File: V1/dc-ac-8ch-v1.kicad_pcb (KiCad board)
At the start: 2 copper layers, 98 x 67.8 mm, 103 parts, among them J1 DB142V-5.08-4P, J2 DB142V-5.08-4P, J3 DB142V-5.08-2P, J4 DB142V-5.08-4P, J5 DB142V-5.08-4P, J6 DB142V-5.08-2P, U1 MOC3063S, U2 MOC3063S, U3 MOC3063S, U4 MOC3063S, U5 MOC3063S, U6 MOC3063S, U7 MOC3063S, U8 MOC3063S

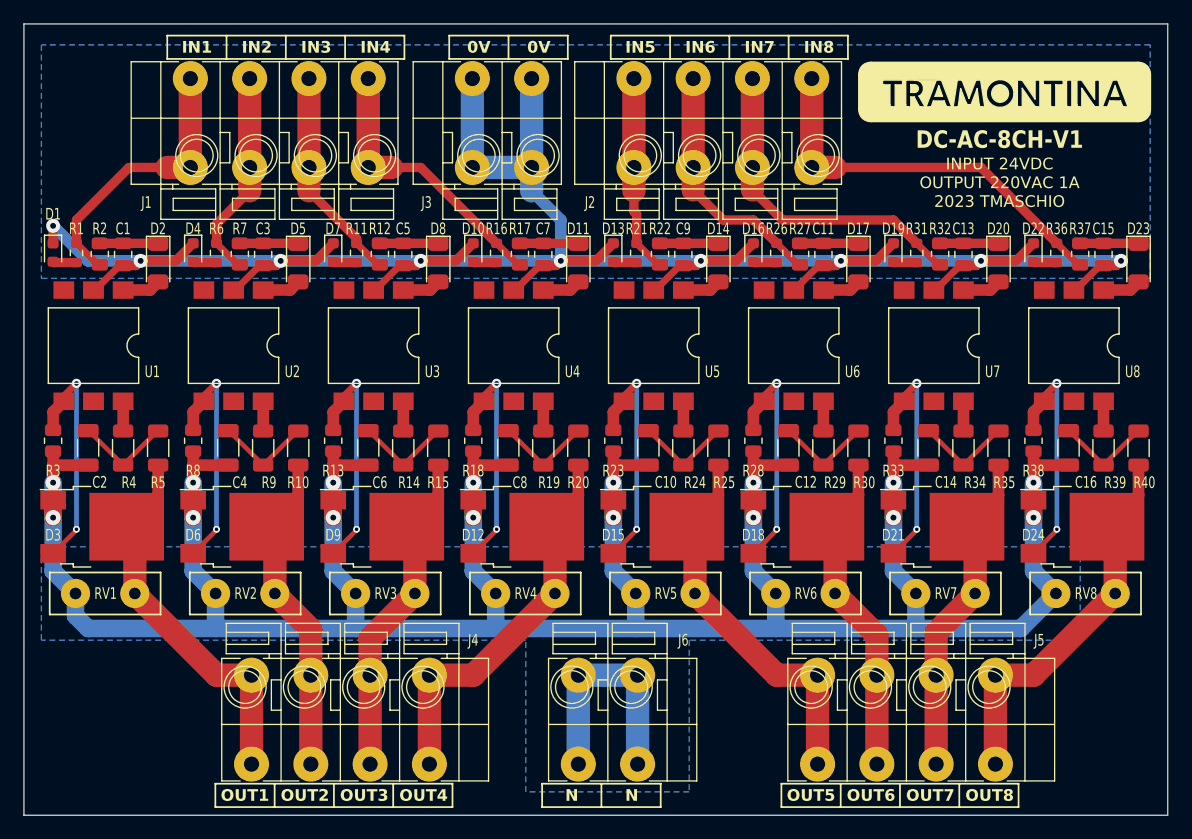
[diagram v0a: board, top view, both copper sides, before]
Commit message: Place missing track under zone
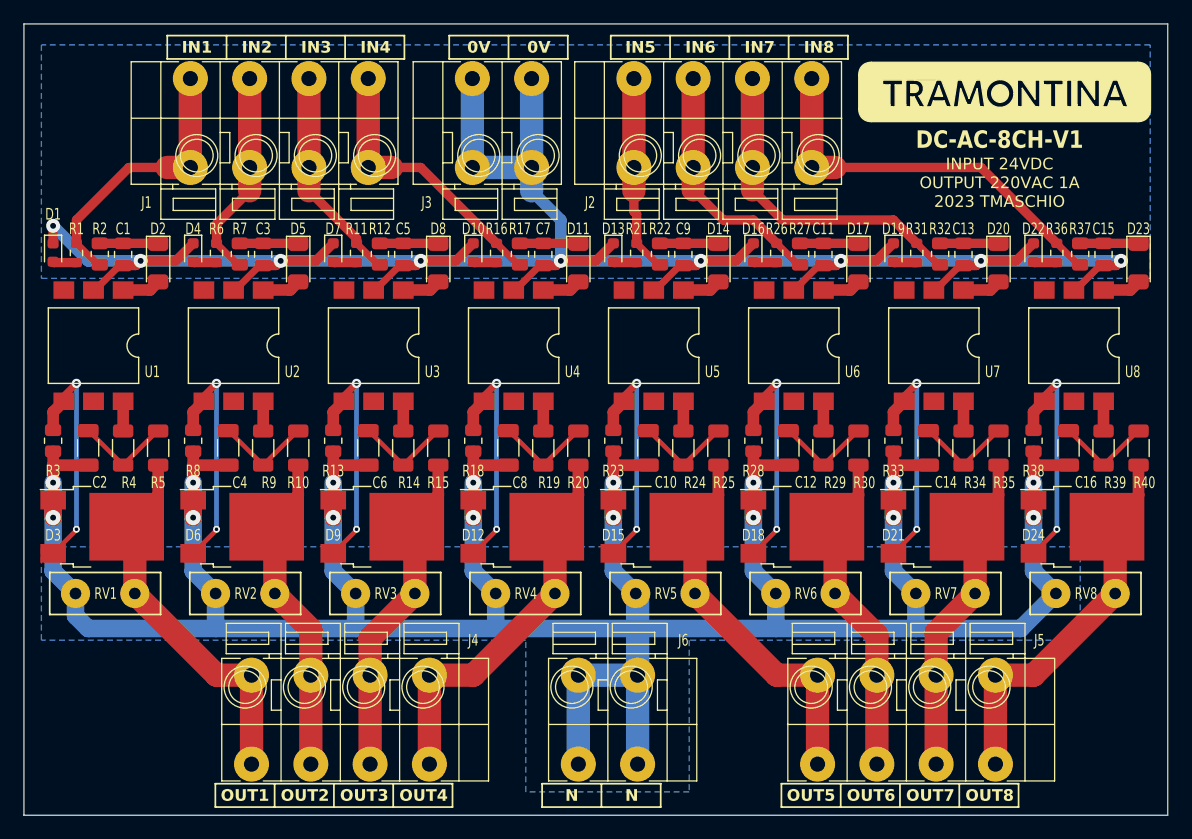
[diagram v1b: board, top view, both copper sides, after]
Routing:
- net NEUTRAL: track 277.7 -> 281.8 mm

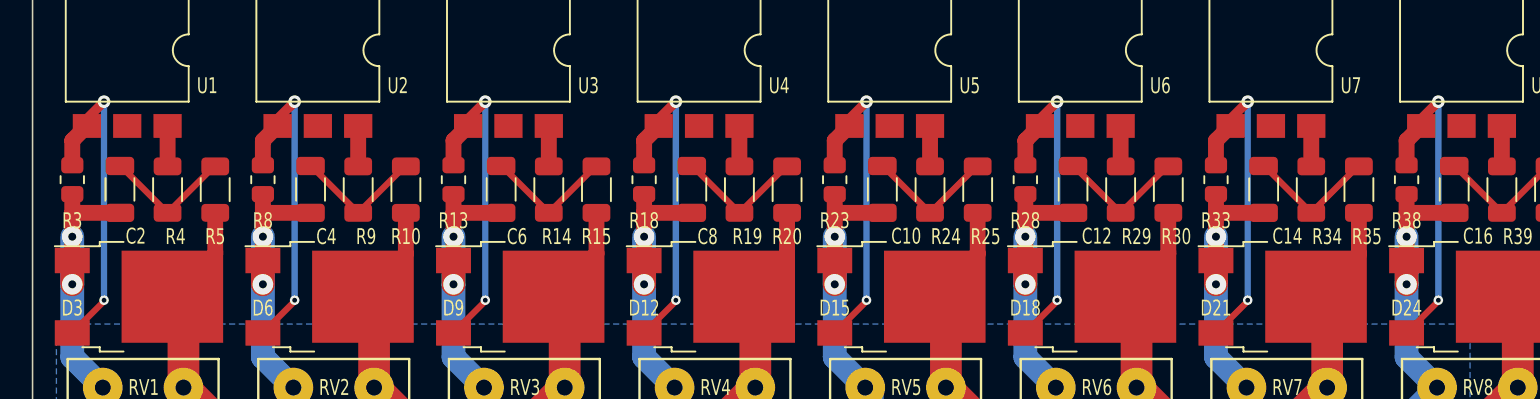
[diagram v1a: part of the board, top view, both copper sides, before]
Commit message: Relocate track
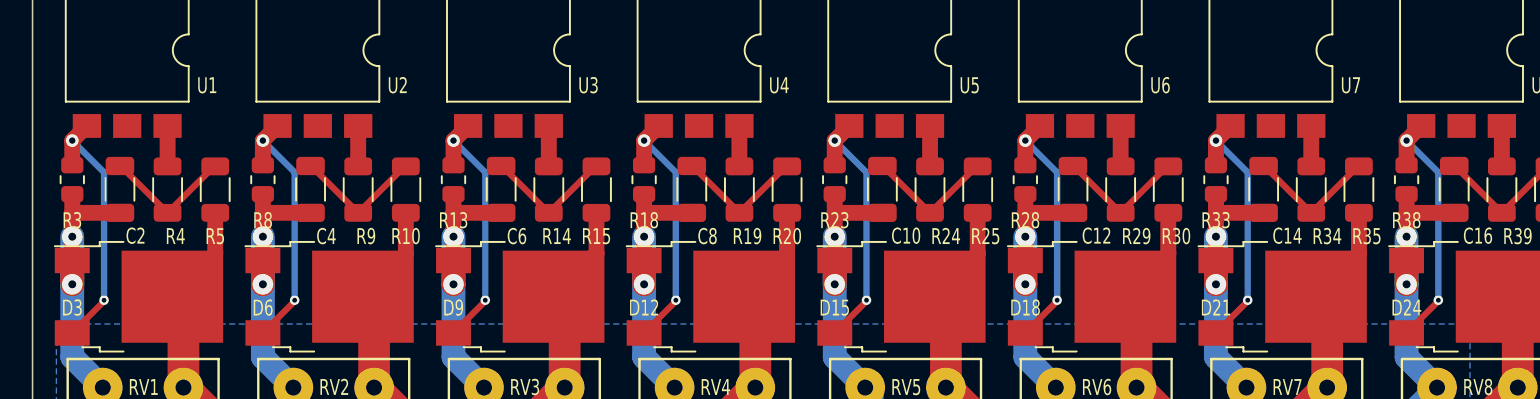
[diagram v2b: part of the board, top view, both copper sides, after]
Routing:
- net Net-(D24-G): track 20.2 -> 16.6 mm
- net Net-(D21-G): track 20.2 -> 16.6 mm
- net Net-(D18-G): track 20.2 -> 16.6 mm
- net Net-(D15-G): track 20.2 -> 16.6 mm
- net Net-(D12-G): track 20.2 -> 16.6 mm
- net Net-(D9-G): track 20.2 -> 16.6 mm
- net Net-(D6-G): track 20.2 -> 16.6 mm
- net Net-(D3-G): track 20.2 -> 16.6 mm
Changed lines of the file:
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@@
   (segment (start 104.5 105.56) (end 102.5 107.56) (width 0.4) (layer "F.Cu") (net 18))
   (segment (start 104.5 105.5) (end 104.5 105.56) (width 0.4) (layer "F.Cu") (net 18))
-  (segment (start 103.42 94.08) (end 103.42 94.53) (width 0.6) (layer "F.Cu") (net 18))
-  (segment (start 104.5 93) (end 103.42 94.08) (width 0.6) (layer "F.Cu") (net 18))
   (segment (start 102.5 95.45) (end 103.42 94.53) (width 1) (layer "F.Cu") (net 18))
   (segment (start 102.5 97) (end 102.5 95.45) (width 1) (layer "F.Cu") (net 18))
-  (via (at 104.5 93) (size 0.8) (drill 0.4) (layers "F.Cu" "B.Cu") (net 18))
+  (via (at 102.5 95.45) (size 0.8) (drill 0.4) (layers "F.Cu" "B.Cu") (net 18))
   (via (at 104.5 105.5) (size 0.6) (drill 0.3) (layers "F.Cu" "B.Cu") (net 18))
-  (segment (start 104.5 93) (end 104.5 105.5) (width 0.4) (layer "B.Cu") (net 18))
+  (segment (start 104.5 97.45) (end 104.5 105.5) (width 0.4) (layer "B.Cu") (net 18))
+  (segment (start 102.5 95.45) (end 104.5 97.45) (width 0.4) (layer "B.Cu") (net 18))
   (segment (start 114.575 82.65) (end 114.5 82.575) (width 0.8) (layer "F.Cu") (net 19))
   (segment (start 116.5 82.65) (end 114.575 82.65) (width 0.8) (layer "F.Cu") (net 19))
@@
   (segment (start 116.5 105.5) (end 116.5 105.56) (width 0.4) (layer "F.Cu") (net 22))
   (segment (start 114.5 95.45) (end 115.42 94.53) (width 1) (layer "F.Cu") (net 22))
-  (segment (start 115.42 94.08) (end 115.42 94.53) (width 0.6) (layer "F.Cu") (net 22))
-  (segment (start 116.5 93) (end 115.42 94.08) (width 0.6) (layer "F.Cu") (net 22))
   (segment (start 116.5 105.56) (end 114.5 107.56) (width 0.4) (layer "F.Cu") (net 22))
   (via (at 116.5 105.5) (size 0.6) (drill 0.3) (layers "F.Cu" "B.Cu") (net 22))
-  (via (at 116.5 93) (size 0.8) (drill 0.4) (layers "F.Cu" "B.Cu") (net 22))
-  (segment (start 116.5 93) (end 116.5 105.5) (width 0.4) (layer "B.Cu") (net 22))
+  (via (at 114.5 95.45) (size 0.8) (drill 0.4) (layers "F.Cu" "B.Cu") (net 22))
+  (segment (start 116.5 97.45) (end 116.5 105.5) (width 0.4) (layer "B.Cu") (net 22))
+  (segment (start 114.5 95.45) (end 116.5 97.45) (width 0.4) (layer "B.Cu") (net 22))
   (segment (start 128.5 82.65) (end 126.575 82.65) (width 0.8) (layer "F.Cu") (net 23))
   (segment (start 126.575 82.65) (end 126.5 82.575) (width 0.8) (layer "F.Cu") (net 23))
@@
   (segment (start 128.5 105.56) (end 126.5 107.56) (width 0.4) (layer "F.Cu") (net 26))
   (segment (start 126.5 97) (end 126.5 95.45) (width 1) (layer "F.Cu") (net 26))
-  (segment (start 128.5 93) (end 127.42 94.08) (width 0.6) (layer "F.Cu") (net 26))
-  (segment (start 127.42 94.08) (end 127.42 94.53) (width 0.6) (layer "F.Cu") (net 26))
-  (via (at 128.5 93) (size 0.8) (drill 0.4) (layers "F.Cu" "B.Cu") (net 26))
   (via (at 128.5 105.5) (size 0.6) (drill 0.3) (layers "F.Cu" "B.Cu") (net 26))
-  (segment (start 128.5 93) (end 128.5 105.5) (width 0.4) (layer "B.Cu") (net 26))
+  (via (at 126.5 95.45) (size 0.8) (drill 0.4) (layers "F.Cu" "B.Cu") (net 26))
+  (segment (start 126.5 95.45) (end 128.5 97.45) (width 0.4) (layer "B.Cu") (net 26))
+  (segment (start 128.5 97.45) (end 128.5 105.5) (width 0.4) (layer "B.Cu") (net 26))
   (segment (start 138.575 82.65) (end 138.5 82.575) (width 0.8) (layer "F.Cu") (net 27))
   (segment (start 140.5 82.65) (end 138.575 82.65) (width 0.8) (layer "F.Cu") (net 27))
@@
   (segment (start 140.5 105.56) (end 138.5 107.56) (width 0.4) (layer "F.Cu") (net 30))
   (segment (start 140.5 105.5) (end 140.5 105.56) (width 0.4) (layer "F.Cu") (net 30))
-  (segment (start 139.42 94.08) (end 139.42 94.53) (width 0.6) (layer "F.Cu") (net 30))
-  (segment (start 140.5 93) (end 139.42 94.08) (width 0.6) (layer "F.Cu") (net 30))
   (segment (start 138.5 97) (end 138.5 95.45) (width 1) (layer "F.Cu") (net 30))
-  (via (at 140.5 93) (size 0.8) (drill 0.4) (layers "F.Cu" "B.Cu") (net 30))
+  (via (at 138.5 95.45) (size 0.8) (drill 0.4) (layers "F.Cu" "B.Cu") (net 30))
   (via (at 140.5 105.5) (size 0.6) (drill 0.3) (layers "F.Cu" "B.Cu") (net 30))
-  (segment (start 140.5 93) (end 140.5 105.5) (width 0.4) (layer "B.Cu") (net 30))
+  (segment (start 138.5 95.45) (end 140.5 97.45) (width 0.4) (layer "B.Cu") (net 30))
+  (segment (start 140.5 97.45) (end 140.5 105.5) (width 0.4) (layer "B.Cu") (net 30))
   (segment (start 150.575 82.65) (end 150.5 82.575) (width 0.8) (layer "F.Cu") (net 31))
   (segment (start 152.5 82.65) (end 150.575 82.65) (width 0.8) (layer "F.Cu") (net 31))
@@
   (segment (start 178.16 118) (end 178.16 114.34) (width 2) (layer "F.Cu") (net 37))
   (segment (start 176.5 105.5) (end 176.5 105.56) (width 0.4) (layer "F.Cu") (net 38))
-  (segment (start 176.5 93) (end 175.42 94.08) (width 0.6) (layer "F.Cu") (net 38))
-  (segment (start 175.42 94.08) (end 175.42 94.53) (width 0.6) (layer "F.Cu") (net 38))
   (segment (start 174.5 95.45) (end 175.42 94.53) (width 1) (layer "F.Cu") (net 38))
   (segment (start 176.5 105.56) (end 174.5 107.56) (width 0.4) (layer "F.Cu") (net 38))
   (segment (start 174.5 97) (end 174.5 95.45) (width 1) (layer "F.Cu") (net 38))
   (via (at 176.5 105.5) (size 0.6) (drill 0.3) (layers "F.Cu" "B.Cu") (net 38))
-  (via (at 176.5 93) (size 0.8) (drill 0.4) (layers "F.Cu" "B.Cu") (net 38))
-  (segment (start 176.5 93) (end 176.5 105.5) (width 0.4) (layer "B.Cu") (net 38))
+  (via (at 174.5 95.45) (size 0.8) (drill 0.4) (layers "F.Cu" "B.Cu") (net 38))
+  (segment (start 176.5 97.45) (end 176.5 105.5) (width 0.4) (layer "B.Cu") (net 38))
+  (segment (start 174.5 95.45) (end 176.5 97.45) (width 0.4) (layer "B.Cu") (net 38))
   (segment (start 186.5 118) (end 193.5 111) (width 2) (layer "F.Cu") (net 39))
   (segment (start 193.5 111) (end 193.5 105.98) (width 2) (layer "F.Cu") (net 39))
@@
   (segment (start 195.5 100) (end 195.5 102.58) (width 1) (layer "F.Cu") (net 39))
   (segment (start 188.5 105.5) (end 188.5 105.56) (width 0.4) (layer "F.Cu") (net 40))
-  (segment (start 188.5 93) (end 187.42 94.08) (width 0.6) (layer "F.Cu") (net 40))
-  (segment (start 187.42 94.08) (end 187.42 94.53) (width 0.6) (layer "F.Cu") (net 40))
   (segment (start 186.5 95.45) (end 187.42 94.53) (width 1) (layer "F.Cu") (net 40))
   (segment (start 186.5 97) (end 186.5 95.45) (width 1) (layer "F.Cu") (net 40))
   (segment (start 188.5 105.56) (end 186.5 107.56) (width 0.4) (layer "F.Cu") (net 40))
   (via (at 188.5 105.5) (size 0.6) (drill 0.3) (layers "F.Cu" "B.Cu") (net 40))
-  (via (at 188.5 93) (size 0.8) (drill 0.4) (layers "F.Cu" "B.Cu") (net 40))
-  (segment (start 188.5 93) (end 188.5 105.5) (width 0.4) (layer "B.Cu") (net 40))
+  (via (at 186.5 95.45) (size 0.8) (drill 0.4) (layers "F.Cu" "B.Cu") (net 40))
+  (segment (start 186.5 95.45) (end 188.5 97.45) (width 0.4) (layer "B.Cu") (net 40))
+  (segment (start 188.5 97.45) (end 188.5 105.5) (width 0.4) (layer "B.Cu") (net 40))
   (segment (start 142.5 82.825) (end 142.325 82.825) (width 0.6) (layer "F.Cu") (net 41))
   (segment (start 129.5 66.88) (end 129.5 74.5) (width 2) (layer "F.Cu") (net 41))
@@
   (segment (start 150.5 95.45) (end 151.42 94.53) (width 1) (layer "F.Cu") (net 71))
   (segment (start 152.5 105.5) (end 152.5 105.56) (width 0.4) (layer "F.Cu") (net 71))
-  (segment (start 152.5 93) (end 151.42 94.08) (width 0.6) (layer "F.Cu") (net 71))
-  (segment (start 151.42 94.08) (end 151.42 94.53) (width 0.6) (layer "F.Cu") (net 71))
   (via (at 152.5 105.5) (size 0.6) (drill 0.3) (layers "F.Cu" "B.Cu") (net 71))
-  (via (at 152.5 93) (size 0.8) (drill 0.4) (layers "F.Cu" "B.Cu") (net 71))
-  (segment (start 152.5 93) (end 152.5 105.5) (width 0.4) (layer "B.Cu") (net 71))
+  (via (at 150.5 95.45) (size 0.8) (drill 0.4) (layers "F.Cu" "B.Cu") (net 71))
+  (segment (start 152.5 97.45) (end 152.5 105.5) (width 0.4) (layer "B.Cu") (net 71))
+  (segment (start 150.5 95.45) (end 152.5 97.45) (width 0.4) (layer "B.Cu") (net 71))
   (segment (start 171.5 100) (end 171.5 102.58) (width 1) (layer "F.Cu") (net 72))
   (segment (start 169.5 111) (end 169.5 105.98) (width 2) (layer "F.Cu") (net 72))
@@
   (segment (start 173.08 125.62) (end 173.08 118) (width 2) (layer "F.Cu") (net 72))
   (segment (start 169.5 105.98) (end 168.8 105.28) (width 2) (layer "F.Cu") (net 72))
-  (segment (start 163.42 94.08) (end 163.42 94.53) (width 0.6) (layer "F.Cu") (net 73))
-  (segment (start 164.5 93) (end 163.42 94.08) (width 0.6) (layer "F.Cu") (net 73))
   (segment (start 164.5 105.56) (end 162.5 107.56) (width 0.4) (layer "F.Cu") (net 73))
   (segment (start 164.5 105.5) (end 164.5 105.56) (width 0.4) (layer "F.Cu") (net 73))
   (segment (start 162.5 97) (end 162.5 95.45) (width 1) (layer "F.Cu") (net 73))
   (segment (start 162.5 95.45) (end 163.42 94.53) (width 1) (layer "F.Cu") (net 73))
+  (via (at 162.5 95.45) (size 0.8) (drill 0.4) (layers "F.Cu" "B.Cu") (net 73))
   (via (at 164.5 105.5) (size 0.6) (drill 0.3) (layers "F.Cu" "B.Cu") (net 73))
-  (via (at 164.5 93) (size 0.8) (drill 0.4) (layers "F.Cu" "B.Cu") (net 73))
-  (segment (start 164.5 93) (end 164.5 105.5) (width 0.4) (layer "B.Cu") (net 73))
+  (segment (start 164.5 97.45) (end 164.5 105.5) (width 0.4) (layer "B.Cu") (net 73))
+  (segment (start 162.5 95.45) (end 164.5 97.45) (width 0.4) (layer "B.Cu") (net 73))
   (segment (start 188.5 82.65) (end 186.575 82.65) (width 0.8) (layer "F.Cu") (net 74))
   (segment (start 186.575 82.65) (end 186.5 82.575) (width 0.8) (layer "F.Cu") (net 74))
